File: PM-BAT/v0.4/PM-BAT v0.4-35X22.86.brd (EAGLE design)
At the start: 35 x 22.9 mm, 87 parts, among them J1 M13PTH-CST-R, J2 M12PTH-CST-R, U1 BQ24195, U2 TPS63020, U3 TPS631011, U5 TPS22918, U6 SPARKFUN-POWERIC_MAX1704X

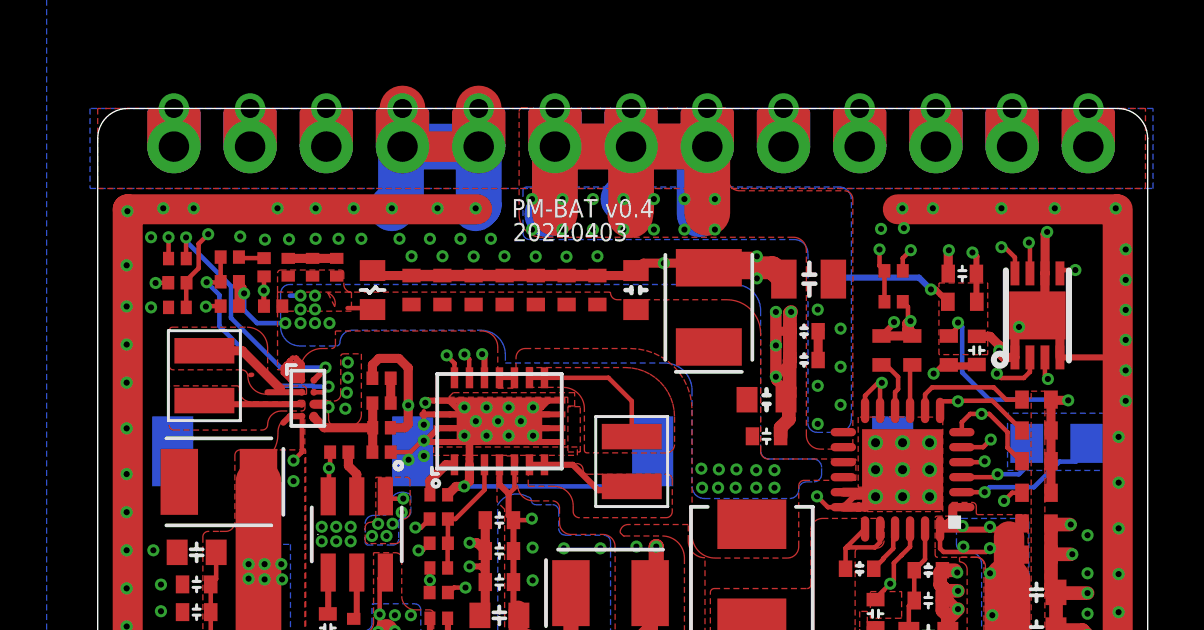
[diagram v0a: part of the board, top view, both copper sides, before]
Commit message: update
output gerber for MO DFM
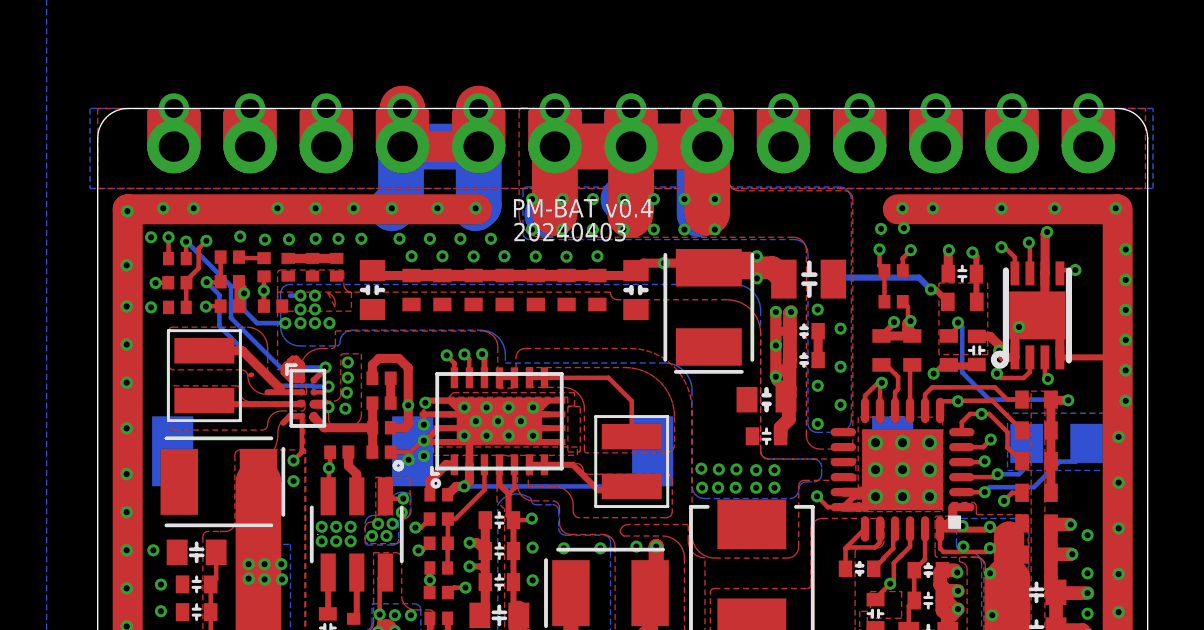
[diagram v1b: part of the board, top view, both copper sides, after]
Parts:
- C12: device particle SZ:R-0603A -> particle SZ:C0603
- L1, L3: value 2.2uH -> 1.5uH
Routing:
- net VSYS: track 13.6 -> 12.8 mm
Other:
- board text added: "3V3 AUX"
